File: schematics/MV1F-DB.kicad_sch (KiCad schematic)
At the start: 4 parts, among them CN1 DIN41612_03x32_AC, CN7 DIN41612_03x32_AC

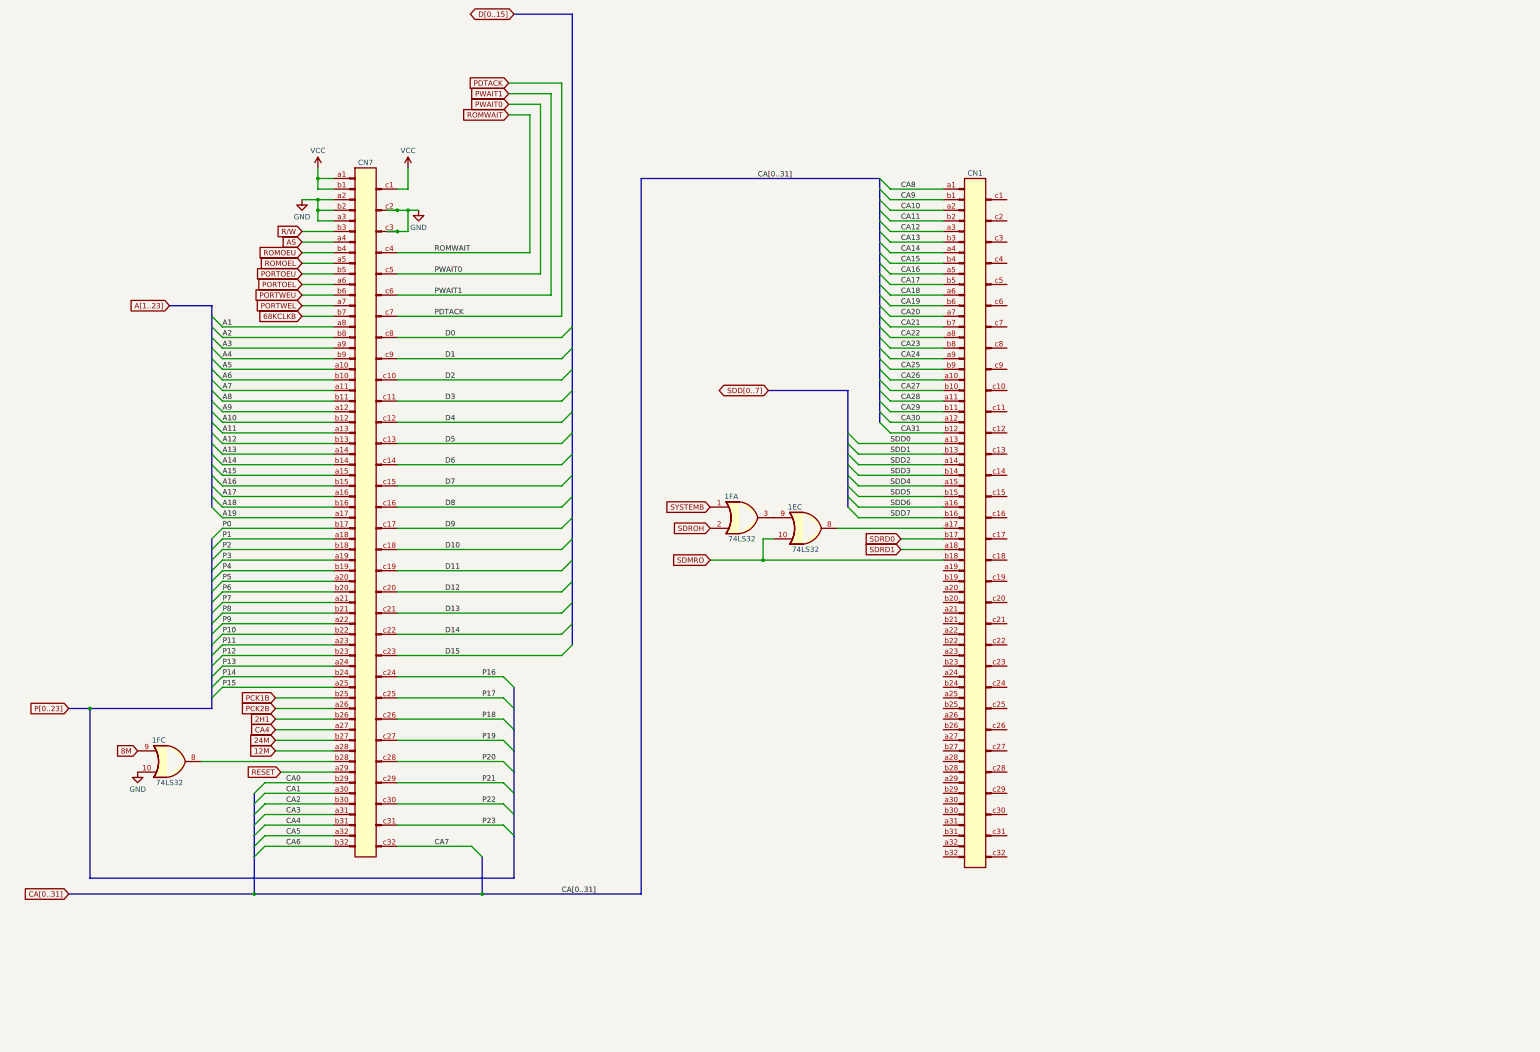
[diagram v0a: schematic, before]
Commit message: complete DaughterBoard
rename sub files
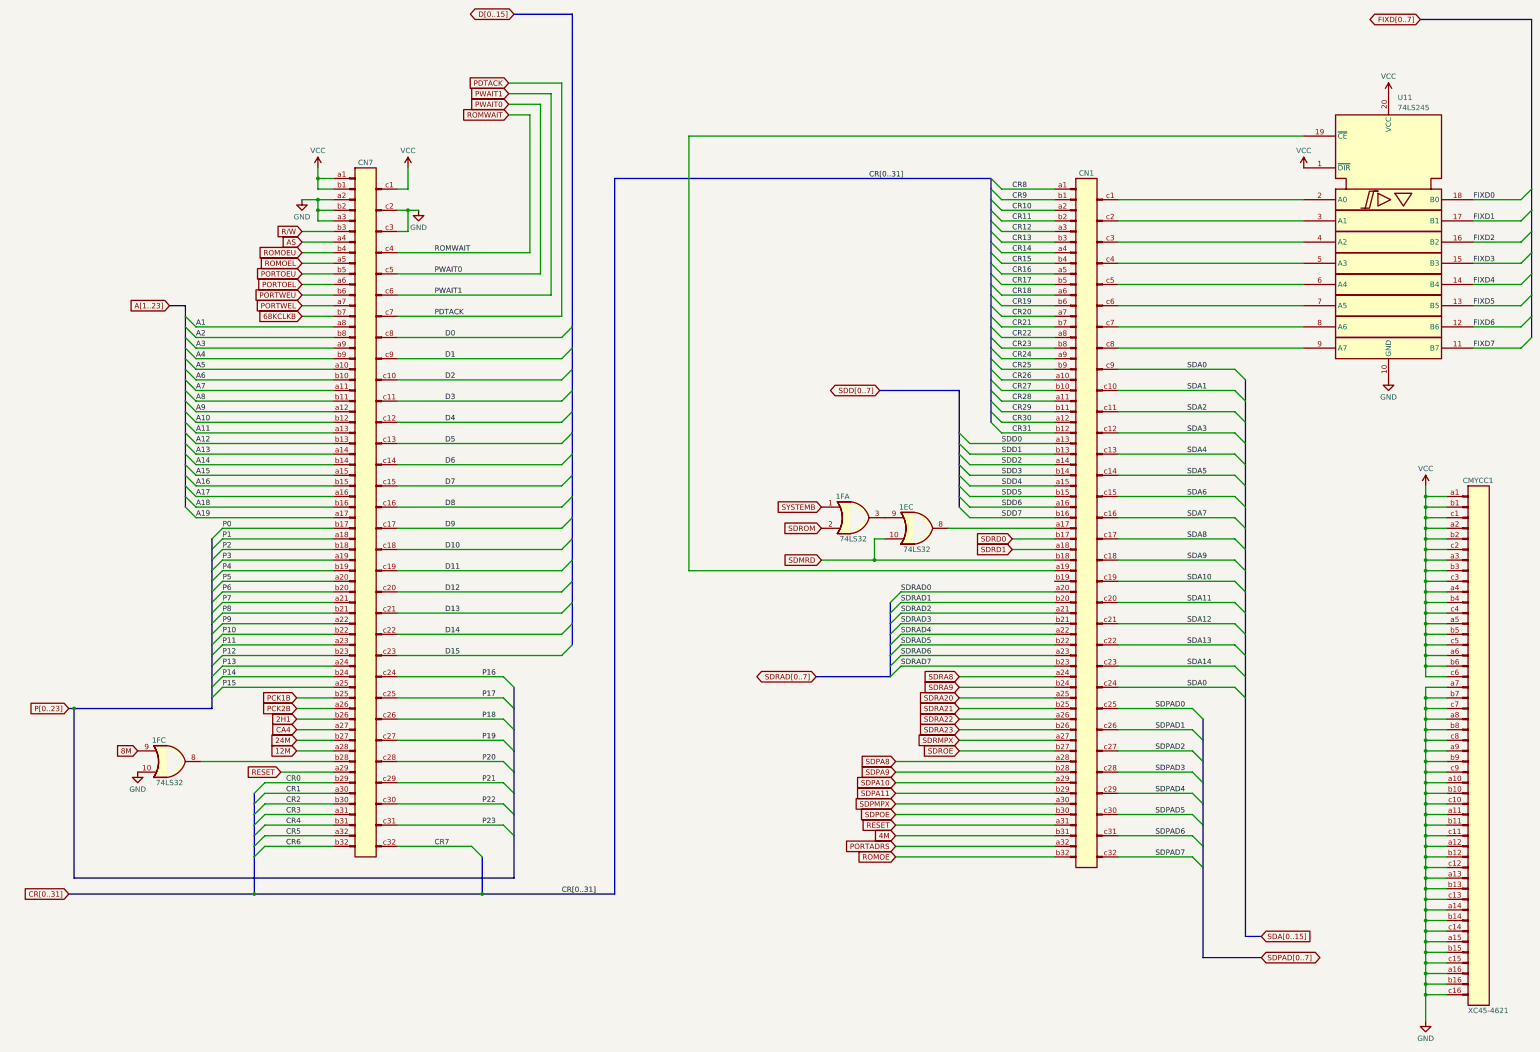
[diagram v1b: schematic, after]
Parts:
- added CMYCC1: XC45-4621, symbol 0-Custom-SNK:DIN41612_03x16_AC-1Row
- added U11: 74LS245, symbol 74xx_IEEE:74LS245
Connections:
- net CA4: no longer CN7.b31 (Pin_a31)
- net GND: now also CMYCC1.a10 (Pin_a10), CMYCC1.a11 (Pin_a11), CMYCC1.a12 (Pin_a12), CMYCC1.a13 (Pin_a13), CMYCC1.a14 (Pin_a14), CMYCC1.a15 (Pin_a15), CMYCC1.a16 (Pin_a16), CMYCC1.a7 (Pin_a7), CMYCC1.a8 (Pin_a8), CMYCC1.a9 (Pin_a9), CMYCC1.b10 (Pin_a10), CMYCC1.b11 (Pin_a11), CMYCC1.b12 (Pin_a12), CMYCC1.b13 (Pin_a13), CMYCC1.b14 (Pin_a14), CMYCC1.b15 (Pin_a15), CMYCC1.b16 (Pin_a16), CMYCC1.b7 (Pin_a7), CMYCC1.b8 (Pin_a8), CMYCC1.b9 (Pin_a9), CMYCC1.c10 (Pin_c10), CMYCC1.c11 (Pin_c11), CMYCC1.c12 (Pin_c12), CMYCC1.c13 (Pin_c13), CMYCC1.c14 (Pin_c14), CMYCC1.c15 (Pin_c15), CMYCC1.c16 (Pin_c16), CMYCC1.c7 (Pin_c7), CMYCC1.c8 (Pin_c8), CMYCC1.c9 (Pin_c9), U11.10 (GND)
- net RESET: now also CN1.a31 (Pin_a31)
- net VCC: now also CMYCC1.a1 (Pin_a1), CMYCC1.a2 (Pin_a2), CMYCC1.a3 (Pin_a3), CMYCC1.a4 (Pin_a4), CMYCC1.a5 (Pin_a5), CMYCC1.a6 (Pin_a6), CMYCC1.b1 (Pin_a1), CMYCC1.b2 (Pin_a2), CMYCC1.b3 (Pin_a3), CMYCC1.b4 (Pin_a4), CMYCC1.b5 (Pin_a5), CMYCC1.b6 (Pin_a6), CMYCC1.c1 (Pin_c1), CMYCC1.c2 (Pin_c2), CMYCC1.c3 (Pin_c3), CMYCC1.c4 (Pin_c4), CMYCC1.c5 (Pin_c5), CMYCC1.c6 (Pin_c6), U11.1 (~{DIR}), U11.20 (VCC)
- net at CN1.a19 (Pin_a19): now also U11.19 (~{CE})
- net SDRAD0: now reaches CN1.a20 (Pin_a20)
- net SDRAD2: now reaches CN1.a21 (Pin_a21)
- net SDRAD4: now reaches CN1.a22 (Pin_a22)
- net SDRAD6: now reaches CN1.a23 (Pin_a23)
- net SDRA8: now reaches CN1.a24 (Pin_a24)
- net SDRA20: now reaches CN1.a25 (Pin_a25)
- net SDRA22: now reaches CN1.a26 (Pin_a26)
- net SDRMPX: now reaches CN1.a27 (Pin_a27)
- net SDPA8: now reaches CN1.a28 (Pin_a28)
- net SDPA10: now reaches CN1.a29 (Pin_a29)
- net SDPMPX: now reaches CN1.a30 (Pin_a30)
- net PORTADRS: now reaches CN1.a32 (Pin_a32)
- net SDRAD1: now reaches CN1.b20 (Pin_a20)
- net SDRAD3: now reaches CN1.b21 (Pin_a21)
- net SDRAD5: now reaches CN1.b22 (Pin_a22)
- net SDRAD7: now reaches CN1.b23 (Pin_a23)
- net SDRA9: now reaches CN1.b24 (Pin_a24)
- net SDRA21: now reaches CN1.b25 (Pin_a25)
- net SDRA23: now reaches CN1.b26 (Pin_a26)
- net SDROE: now reaches CN1.b27 (Pin_a27)
- net SDPA9: now reaches CN1.b28 (Pin_a28)
- net SDPA11: now reaches CN1.b29 (Pin_a29)
- net SDPOE: now reaches CN1.b30 (Pin_a30)
- net 4M: now reaches CN1.b31 (Pin_a31)
- net ROMOE: now reaches CN1.b32 (Pin_a32)
- net at CN1.c1 (Pin_c1): now also U11.2 (A0)
- net SDA1: now reaches CN1.c10 (Pin_c10)
- net SDA2: now reaches CN1.c11 (Pin_c11)
- net SDA3: now reaches CN1.c12 (Pin_c12)
- net SDA4: now reaches CN1.c13 (Pin_c13)
- net SDA5: now reaches CN1.c14 (Pin_c14)
- net SDA6: now reaches CN1.c15 (Pin_c15)
- net SDA7: now reaches CN1.c16 (Pin_c16)
- net SDA8: now reaches CN1.c17 (Pin_c17)
- net SDA9: now reaches CN1.c18 (Pin_c18)
- net SDA10: now reaches CN1.c19 (Pin_c19)
- net at CN1.c2 (Pin_c2): now also U11.3 (A1)
- net SDA11: now reaches CN1.c20 (Pin_c20)
- net SDA12: now reaches CN1.c21 (Pin_c21)
- net SDA13: now reaches CN1.c22 (Pin_c22)
- net SDA14: now reaches CN1.c23 (Pin_c23)
- net SDA0: now reaches CN1.c24 (Pin_c24)
- net SDA0: now also CN1.c9 (Pin_c9)
- net SDPAD0: now reaches CN1.c25 (Pin_c25)
- net SDPAD1: now reaches CN1.c26 (Pin_c26)
- net SDPAD2: now reaches CN1.c27 (Pin_c27)
- net SDPAD3: now reaches CN1.c28 (Pin_c28)
- net SDPAD4: now reaches CN1.c29 (Pin_c29)
- net at CN1.c3 (Pin_c3): now also U11.4 (A2)
- net SDPAD5: now reaches CN1.c30 (Pin_c30)
- net SDPAD6: now reaches CN1.c31 (Pin_c31)
- net SDPAD7: now reaches CN1.c32 (Pin_c32)
- net at CN1.c4 (Pin_c4): now also U11.5 (A3)
- net at CN1.c5 (Pin_c5): now also U11.6 (A4)
- net at CN1.c6 (Pin_c6): now also U11.7 (A5)
- net at CN1.c7 (Pin_c7): now also U11.8 (A6)
- net at CN1.c8 (Pin_c8): now also U11.9 (A7)
- net CA0 renamed CR0
- net CA1 renamed CR1
- net CA10 renamed CR10
- net CA11 renamed CR11
- net CA12 renamed CR12
- net CA13 renamed CR13
- net CA14 renamed CR14
- net CA15 renamed CR15
- net CA16 renamed CR16
- net CA17 renamed CR17
- net CA18 renamed CR18
- net CA19 renamed CR19
- net CA2 renamed CR2
- net CA20 renamed CR20
- net CA21 renamed CR21
- net CA22 renamed CR22
- net CA23 renamed CR23
- net CA24 renamed CR24
- net CA25 renamed CR25
- net CA26 renamed CR26
- net CA27 renamed CR27
- net CA28 renamed CR28
- net CA29 renamed CR29
- net CA3 renamed CR3
- net CA30 renamed CR30
- net CA31 renamed CR31
- net CA5 renamed CR5
- net CA6 renamed CR6
- net CA7 renamed CR7
- net CA8 renamed CR8
- net CA9 renamed CR9
- net SDMRO renamed SDMRD
- net SDROH renamed SDROM
- new net CR4: CN7.b31 (Pin_a31)
- new net FIXD0: U11.18 (B0)
- new net FIXD1: U11.17 (B1)
- new net FIXD2: U11.16 (B2)
- new net FIXD3: U11.15 (B3)
- new net FIXD4: U11.14 (B4)
- new net FIXD5: U11.13 (B5)
- new net FIXD6: U11.12 (B6)
- new net FIXD7: U11.11 (B7)
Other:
- title: (none) -> Daughterboard connectors
- moved on the sheet: 1EC, 1FA, CN1
